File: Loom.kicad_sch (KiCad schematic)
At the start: 6 parts, among them U2 Camshaft Position Sensor, U3 Crank Position Sensor, U4 Manifold Absolute Pressure Se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

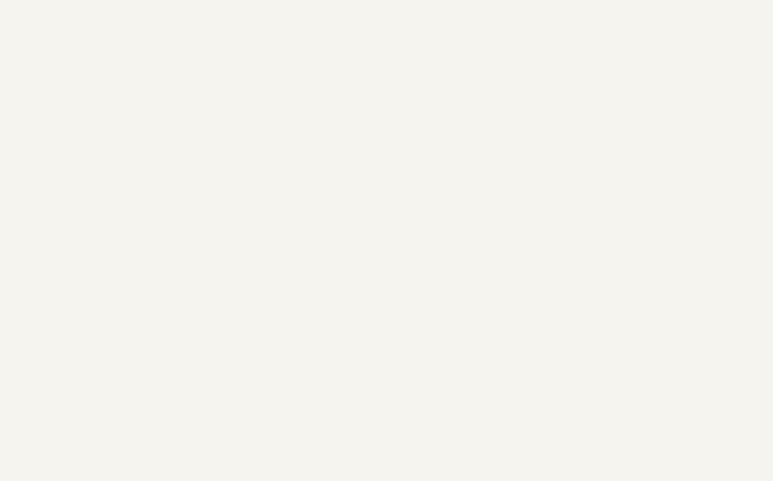
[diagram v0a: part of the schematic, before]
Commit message: Add BSPD as a submodule
Signed-off-by: Oliver Gaskell <og305@cam.ac.uk>
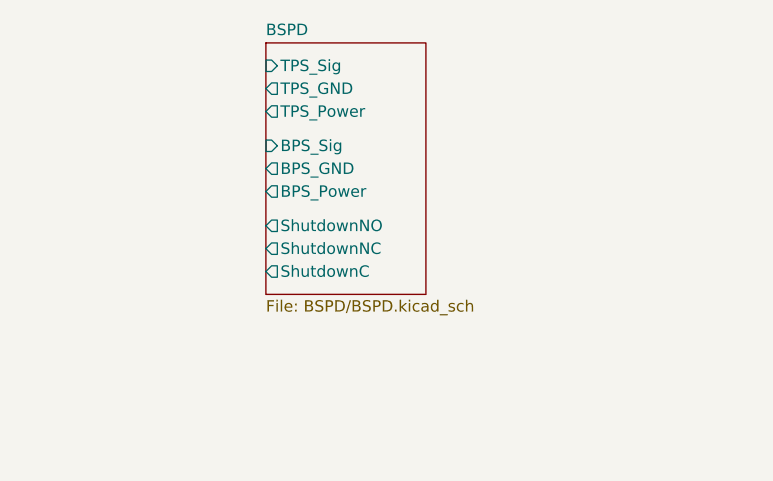
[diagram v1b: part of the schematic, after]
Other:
- added sheet BSPD (BSPD/BSPD.kicad_sch)
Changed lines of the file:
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@@
 	)
 	(symbol
-		(lib_name "FBR_Symbols:Sen_1p_5V")
 		(lib_id "FBR_Symbols:Sen_1p_5V")
 		(at 224.79 87.63 0)
@@
 				)
 			)
+		)
+	)
+	(sheet
+		(at 215.9 26.67)
+		(size 17.78 27.94)
+		(fields_autoplaced yes)
+		(stroke
+			(width 0.1524)
+			(type solid)
+		)
+		(fill
+			(color 0 0 0 0.0000)
+		)
+		(property "Sheetname" "BSPD"
+			(at 215.9 25.9584 0)
+			(effects
+				(font
+					(size 1.27 1.27)
+				)
+				(justify left bottom)
+			)
+		)
+		(property "Sheetfile" "BSPD/BSPD.kicad_sch"
+			(at 215.9 55.1946 0)
+			(effects
+				(font
+					(size 1.27 1.27)
+				)
+				(justify left top)
+			)
+		)
+		(pin "TPS_Sig" input
+			(at 215.9 29.21 180)
+			(effects
+				(font
+					(size 1.27 1.27)
+				)
+				(justify left)
+			)
+		)
+		(pin "TPS_GND" output
+			(at 215.9 31.75 180)
+			(effects
+				(font
+					(size 1.27 1.27)
+				)
+				(justify left)
+			)
+		)
+		(pin "TPS_Power" output
+			(at 215.9 34.29 180)
+			(effects
+				(font
+					(size 1.27 1.27)
+				)
+				(justify left)
+			)
+		)
+		(pin "BPS_Sig" input
+			(at 215.9 38.1 180)
+			(effects
+				(font
+					(size 1.27 1.27)
+				)
+				(justify left)
+			)
+		)
+		(pin "BPS_GND" output
+			(at 215.9 40.64 180)
+			(effects
+				(font
+					(size 1.27 1.27)
+				)
+				(justify left)
+			)
+		)
+		(pin "ShutdownNO" output
+			(at 215.9 46.99 180)
+			(effects
+				(font
+					(size 1.27 1.27)
+				)
+				(justify left)
+			)
+		)
+		(pin "ShutdownNC" output
+			(at 215.9 49.53 180)
+			(effects
+				(font
+					(size 1.27 1.27)
+				)
+				(justify left)
+			)
+		)
+		(pin "ShutdownC" output
+			(at 215.9 52.07 180)
+			(effects
+				(font
+					(size 1.27 1.27)
+				)
+				(justify left)
+			)
+		)
+		(pin "BPS_Power" output
+			(at 215.9 43.18 180)
+			(effects
+				(font
+					(size 1.27 1.27)
+				)
+				(justify left)
+			)
+		)
+		(instances
+			(project "Loom"
+				(path "/fd7e6037-b3ae-4db3-a782-011f61b6fc75"
+					(page "2")
+				)
+			)

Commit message: Misc changes
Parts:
- added BT1: 12V Battery, symbol Device:Battery
- added F1: Fuse, symbol Device:Fuse
- added IN1, IN2, IN3, IN4: Injector, symbol FBR_Symbols:Injector
- added K1: Starter Relay, symbol Relay:Relay_SPST-NO
- added SW1: LVMS, symbol Switch:SW_SPST
- added SW2: ESTOP L, symbol Switch:SW_SPST
- added SW3: ESTOP R, symbol Switch:SW_SPST
- added SW4: ESTOP Driver, symbol Switch:SW_SPST
- added SW5: Inertia Switch, symbol Switch:SW_SPST
- added SW6: BOTS, symbol Switch:SW_SPST
- added U5: Lambda Sensor, symbol FBR_Symbols:Sen_1p_12V
- added U6: TPS, symbol FBR_Symbols:Sen_1p_5V
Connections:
- net BSPD/ShutdownNO: now also SW4.2 (B)
- new net: SW2.1 (A), SW5.2 (B)
- new net: SW2.2 (B), SW3.1 (A)
- new net: SW5.1 (A), SW6.2 (B)
- new net: SW3.2 (B), SW4.1 (A)
- new net BATT+: BT1.1 (+), F1.2
- new net BATT_LVMS: F1.1, SW1.1 (A)
- new net CAR_LVMS: SW1.2 (B)
- new net GND: BT1.2 (-)
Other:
- added sheet Fusebox (Fusebox.kicad_sch)
- note added: "< 100mm"
- note added: "NOTES: - GND symbol is used to represent grounding to the chassis. This should be done with a ring terminal."
- moved on the sheet: U1, U2
